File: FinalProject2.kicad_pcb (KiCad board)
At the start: 2 copper layers, 48.3 x 91.4 mm, 22 parts, among them P1 Conn_01x03, P2 Conn_01x02, P3 Conn_01x04, U1 L78L05_TO92, U2 LM339

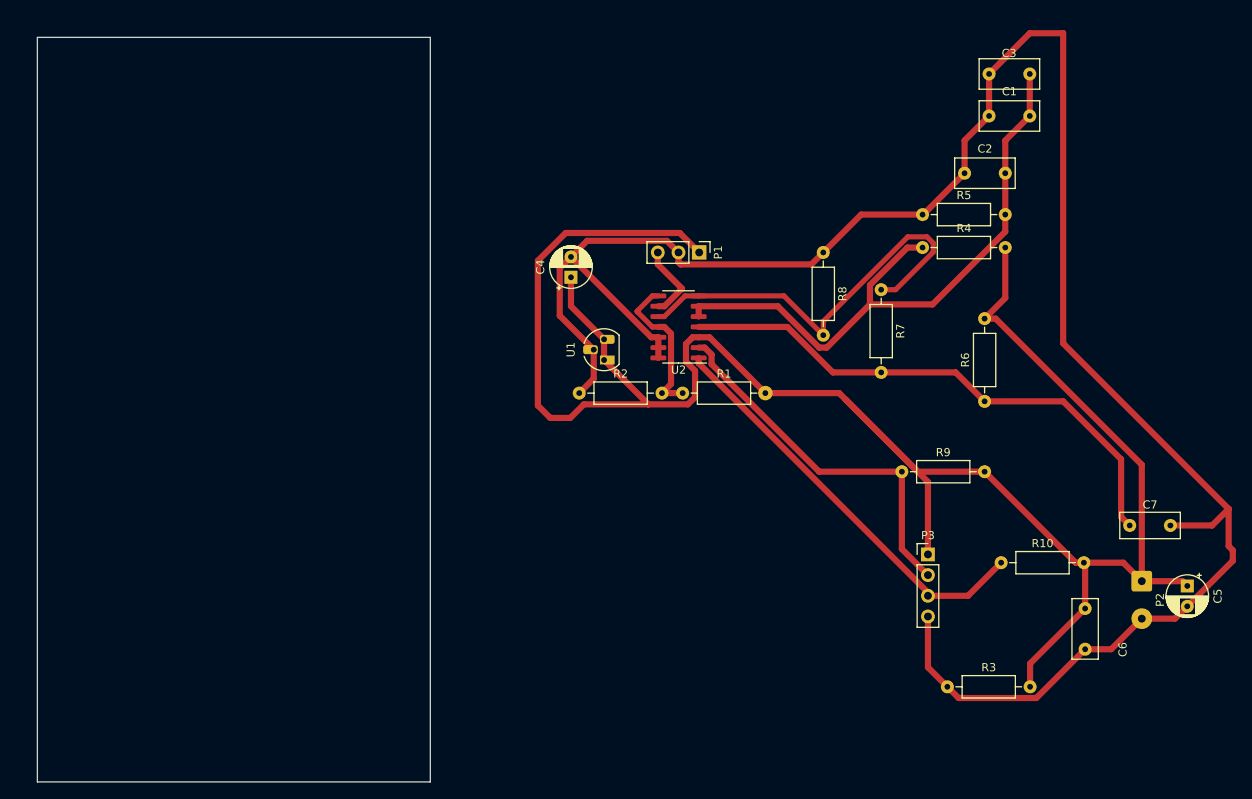
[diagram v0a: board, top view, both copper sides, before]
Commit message: GRN thickness changed to 40mils
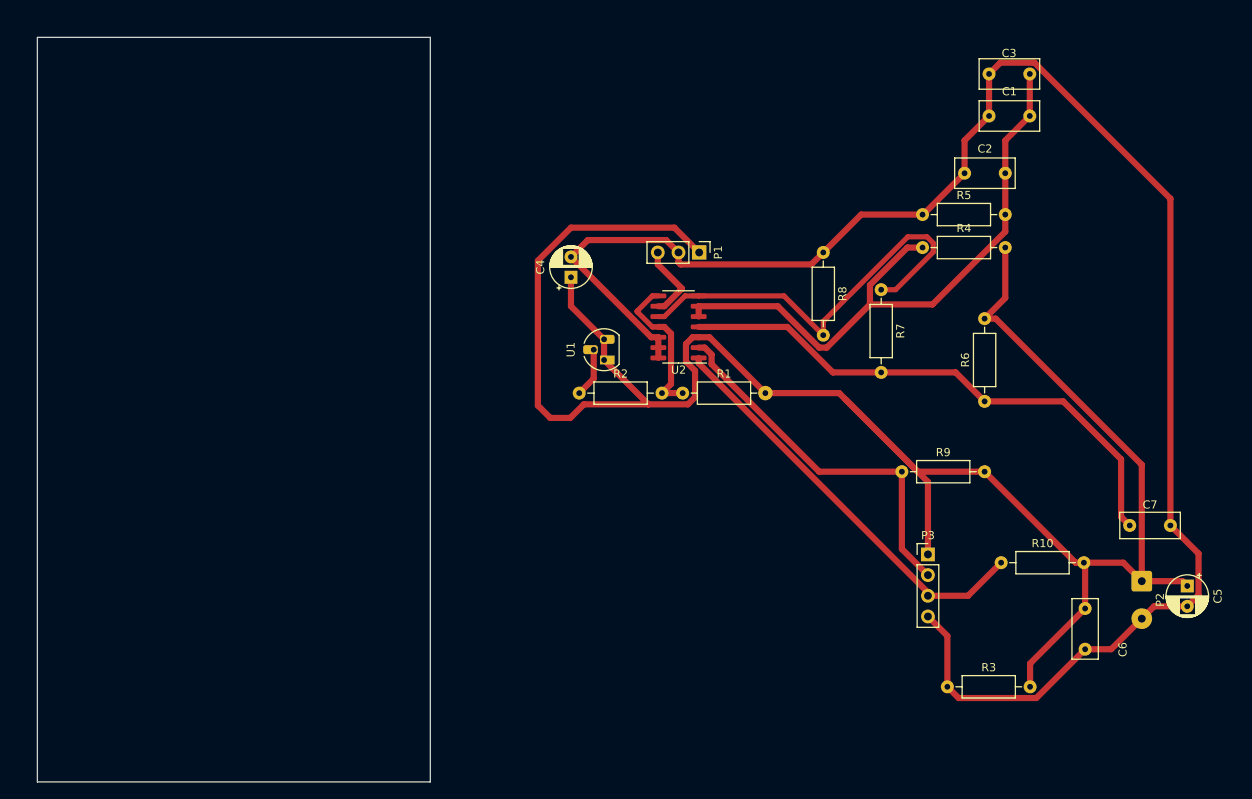
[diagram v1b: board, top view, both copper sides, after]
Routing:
- net GND: track 251.1 -> 218.8 mm
- net Net-(P1-Pin_1): track 254.2 -> 254.8 mm

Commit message: may nakaligtaan akong 1 wire asdasdadsf
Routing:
- net GND: track 218.8 -> 232.5 mm
- net Net-(U2C-+): track 19.0 -> 18.2 mm
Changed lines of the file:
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@@
   (segment (start 277.225 119.293888) (end 275.844 120.674888) (width 0.762) (layer "F.Cu") (net 3))
   (segment (start 270.256 122.188) (end 266.5 125.944) (width 0.762) (layer "F.Cu") (net 3))
+  (segment (start 202.946 89.154) (end 198.771 84.979) (width 0.762) (layer "F.Cu") (net 3))
   (segment (start 202.946 92.71) (end 201.168 94.488) (width 0.762) (layer "F.Cu") (net 3))
+  (segment (start 198.771 84.979) (end 198.771 79.145) (width 0.762) (layer "F.Cu") (net 3))
   (segment (start 231.14 77.216) (end 235.792 72.564) (width 0.762) (layer "F.Cu") (net 3))
   (segment (start 246.38 130.556) (end 246.38 124.306) (width 0.762) (layer "F.Cu") (net 3))
@@
   (segment (start 248.492 63.46) (end 251.5 60.452) (width 0.762) (layer "F.Cu") (net 3))
   (segment (start 210.885 90.17) (end 210.885 87.63) (width 0.762) (layer "F.Cu") (net 3))
+  (segment (start 198.771 79.145) (end 200.152 77.764) (width 0.762) (layer "F.Cu") (net 3))
   (segment (start 251.5 55.292) (end 252.881 53.911) (width 0.762) (layer "F.Cu") (net 3))
   (segment (start 211.836 75.692) (end 213.36 77.216) (width 0.762) (layer "F.Cu") (net 3))
@@
   (segment (start 248.92 119.38) (end 252.984 115.316) (width 0.762) (layer "F.Cu") (net 7))
   (segment (start 215.835 90.818316) (end 243.994 118.977316) (width 0.762) (layer "F.Cu") (net 7))
-  (segment (start 210.14621 86.36) (end 210.885 86.36) (width 0.635) (layer "F.Cu") (net 8))
   (segment (start 211.328 94.488) (end 212.441 93.375) (width 0.762) (layer "F.Cu") (net 8))
   (segment (start 212.441 93.375) (end 212.441 87.17721) (width 0.762) (layer "F.Cu") (net 8))
+  (segment (start 210.885 82.55) (end 210.14621 82.55) (width 0.762) (layer "F.Cu") (net 8))
+  (segment (start 210.14621 82.55) (end 209.296 83.40021) (width 0.762) (layer "F.Cu") (net 8))
   (segment (start 212.441 87.17721) (end 211.62379 86.36) (width 0.762) (layer "F.Cu") (net 8))
-  (segment (start 208.28 84.41621) (end 208.28 84.49379) (width 0.635) (layer "F.Cu") (net 8))
-  (segment (start 210.14621 82.55) (end 208.28 84.41621) (width 0.635) (layer "F.Cu") (net 8))
-  (segment (start 210.885 82.55) (end 210.14621 82.55) (width 0.635) (layer "F.Cu") (net 8))
   (segment (start 213.868 94.488) (end 211.328 94.488) (width 0.762) (layer "F.Cu") (net 8))
   (segment (start 211.62379 86.36) (end 210.885 86.36) (width 0.762) (layer "F.Cu") (net 8))
-  (segment (start 208.28 84.49379) (end 210.14621 86.36) (width 0.635) (layer "F.Cu") (net 8))
-  (segment (start 241.519801 75.2965) (end 243.877727 75.2965) (width 0.635) (layer "F.Cu") (net 9))
-  (segment (start 244.6495 76.068273) (end 244.6495 77.159727) (width 0.635) (layer "F.Cu") (net 9))
-  (segment (start 231.14 85.676301) (end 241.519801 75.2965) (width 0.635) (layer "F.Cu") (net 9))
-  (segment (start 214.16379 82.55) (end 211.62379 85.09) (width 0.635) (layer "F.Cu") (net 9))
-  (segment (start 226.314 82.55) (end 231.14 87.376) (width 0.635) (layer "F.Cu") (net 9))
-  (segment (start 215.835 82.55) (end 214.16379 82.55) (width 0.635) (layer "F.Cu") (net 9))
-  (segment (start 211.62379 85.09) (end 210.885 85.09) (width 0.635) (layer "F.Cu") (net 9))
-  (segment (start 231.14 87.376) (end 231.14 85.676301) (width 0.635) (layer "F.Cu") (net 9))
-  (segment (start 215.835 82.55) (end 226.314 82.55) (width 0.635) (layer "F.Cu") (net 9))
-  (segment (start 244.6495 77.159727) (end 240.021227 81.788) (width 0.635) (layer "F.Cu") (net 9))
-  (segment (start 243.877727 75.2965) (end 244.6495 76.068273) (width 0.635) (layer "F.Cu") (net 9))
-  (segment (start 240.021227 81.788) (end 238.252 81.788) (width 0.635) (layer "F.Cu") (net 9))
+  (segment (start 210.108474 86.36) (end 210.885 86.36) (width 0.762) (layer "F.Cu") (net 8))
+  (segment (start 209.296 83.40021) (end 209.296 85.547526) (width 0.762) (layer "F.Cu") (net 8))
+  (segment (start 209.296 85.547526) (end 210.108474 86.36) (width 0.762) (layer "F.Cu") (net 8))
+  (segment (start 243.904029 75.233) (end 244.713 76.041971) (width 0.762) (layer "F.Cu") (net 9))
+  (segment (start 215.09621 82.55) (end 215.835 82.55) (width 0.762) (layer "F.Cu") (net 9))
+  (segment (start 241.493498 75.233) (end 243.904029 75.233) (width 0.762) (layer "F.Cu") (net 9))
+  (segment (start 240.116029 81.788) (end 238.252 81.788) (width 0.762) (layer "F.Cu") (net 9))
+  (segment (start 212.55621 85.09) (end 215.09621 82.55) (width 0.762) (layer "F.Cu") (net 9))
+  (segment (start 244.713 76.041971) (end 244.713 77.191029) (width 0.762) (layer "F.Cu") (net 9))
+  (segment (start 210.885 85.09) (end 212.55621 85.09) (width 0.762) (layer "F.Cu") (net 9))
+  (segment (start 231.14 85.586498) (end 241.493498 75.233) (width 0.762) (layer "F.Cu") (net 9))
+  (segment (start 231.14 87.376) (end 231.14 85.586498) (width 0.762) (layer "F.Cu") (net 9))
+  (segment (start 226.314 82.55) (end 231.14 87.376) (width 0.762) (layer "F.Cu") (net 9))
+  (segment (start 215.835 82.55) (end 226.314 82.55) (width 0.762) (layer "F.Cu") (net 9))
+  (segment (start 244.713 77.191029) (end 240.116029 81.788) (width 0.762) (layer "F.Cu") (net 9))
 )

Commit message: 40 na yung GRD(2)
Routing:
- net GND: track 232.5 -> 234.9 mm
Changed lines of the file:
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@@
   (segment (start 270.256 103.287527) (end 270.256 117.588) (width 0.762) (layer "F.Cu") (net 2))
   (segment (start 200.152 83.82) (end 204.216 87.884) (width 0.762) (layer "F.Cu") (net 2))
-  (segment (start 277.225 114.197) (end 277.225 119.293888) (width 0.762) (layer "F.Cu") (net 3))
-  (segment (start 273.772 70.610971) (end 273.772 110.744) (width 0.762) (layer "F.Cu") (net 3))
-  (segment (start 213.627919 78.686) (end 229.67 78.686) (width 0.762) (layer "F.Cu") (net 3))
-  (segment (start 251.5 60.452) (end 251.5 55.292) (width 0.762) (layer "F.Cu") (net 3))
-  (segment (start 210.018 87.63) (end 210.885 87.63) (width 0.762) (layer "F.Cu") (net 3))
-  (segment (start 277.225 119.293888) (end 275.844 120.674888) (width 0.762) (layer "F.Cu") (net 3))
-  (segment (start 270.256 122.188) (end 266.5 125.944) (width 0.762) (layer "F.Cu") (net 3))
-  (segment (start 202.946 89.154) (end 198.771 84.979) (width 0.762) (layer "F.Cu") (net 3))
-  (segment (start 202.946 92.71) (end 201.168 94.488) (width 0.762) (layer "F.Cu") (net 3))
-  (segment (start 198.771 84.979) (end 198.771 79.145) (width 0.762) (layer "F.Cu") (net 3))
-  (segment (start 231.14 77.216) (end 235.792 72.564) (width 0.762) (layer "F.Cu") (net 3))
-  (segment (start 246.38 130.556) (end 246.38 124.306) (width 0.762) (layer "F.Cu") (net 3))
-  (segment (start 213.36 78.418081) (end 213.627919 78.686) (width 0.762) (layer "F.Cu") (net 3))
-  (segment (start 202.224 75.692) (end 211.836 75.692) (width 0.762) (layer "F.Cu") (net 3))
-  (segment (start 243.332 72.564) (end 243.412 72.564) (width 0.762) (layer "F.Cu") (net 3))
-  (segment (start 252.881 53.911) (end 257.072029 53.911) (width 0.762) (layer "F.Cu") (net 3))
-  (segment (start 202.946 89.154) (end 202.946 92.71) (width 0.762) (layer "F.Cu") (net 3))
-  (segment (start 213.36 77.216) (end 213.36 78.418081) (width 0.762) (layer "F.Cu") (net 3))
-  (segment (start 229.67 78.686) (end 231.14 77.216) (width 0.762) (layer "F.Cu") (net 3))
-  (segment (start 257.072029 53.911) (end 273.772 70.610971) (width 0.762) (layer "F.Cu") (net 3))
-  (segment (start 247.761 131.937) (end 246.38 130.556) (width 0.762) (layer "F.Cu") (net 3))
-  (segment (start 275.844 120.674888) (end 271.769112 120.674888) (width 0.762) (layer "F.Cu") (net 3))
-  (segment (start 243.412 72.564) (end 248.492 67.484) (width 0.762) (layer "F.Cu") (net 3))
-  (segment (start 273.772 110.744) (end 277.225 114.197) (width 0.762) (layer "F.Cu") (net 3))
-  (segment (start 235.792 72.564) (end 243.332 72.564) (width 0.762) (layer "F.Cu") (net 3))
-  (segment (start 246.38 124.306) (end 243.994 121.92) (width 0.762) (layer "F.Cu") (net 3))
-  (segment (start 271.769112 120.674888) (end 270.256 122.188) (width 0.762) (layer "F.Cu") (net 3))
-  (segment (start 200.152 77.764) (end 210.018 87.63) (width 0.762) (layer "F.Cu") (net 3))
-  (segment (start 200.152 77.764) (end 202.224 75.692) (width 0.762) (layer "F.Cu") (net 3))
-  (segment (start 263.298 125.944) (end 257.305 131.937) (width 0.762) (layer "F.Cu") (net 3))
-  (segment (start 248.492 67.484) (end 248.492 63.46) (width 0.762) (layer "F.Cu") (net 3))
-  (segment (start 257.305 131.937) (end 247.761 131.937) (width 0.762) (layer "F.Cu") (net 3))
-  (segment (start 248.492 63.46) (end 251.5 60.452) (width 0.762) (layer "F.Cu") (net 3))
-  (segment (start 210.885 90.17) (end 210.885 87.63) (width 0.762) (layer "F.Cu") (net 3))
-  (segment (start 198.771 79.145) (end 200.152 77.764) (width 0.762) (layer "F.Cu") (net 3))
-  (segment (start 251.5 55.292) (end 252.881 53.911) (width 0.762) (layer "F.Cu") (net 3))
-  (segment (start 211.836 75.692) (end 213.36 77.216) (width 0.762) (layer "F.Cu") (net 3))
-  (segment (start 266.5 125.944) (end 263.298 125.944) (width 0.762) (layer "F.Cu") (net 3))
+  (segment (start 253.008 53.784) (end 257.124635 53.784) (width 1.016) (layer "F.Cu") (net 3))
+  (segment (start 201.168 90.932) (end 202.946 89.154) (width 1.016) (layer "F.Cu") (net 3))
+  (segment (start 248.492 67.484) (end 248.492 63.46) (width 1.016) (layer "F.Cu") (net 3))
+  (segment (start 257.178 132.064) (end 247.888 132.064) (width 1.016) (layer "F.Cu") (net 3))
+  (segment (start 275.844 120.674888) (end 271.769112 120.674888) (width 1.016) (layer "F.Cu") (net 3))
+  (segment (start 208.207 84.68763) (end 208.207 85.998604) (width 1.016) (layer "F.Cu") (net 3))
+  (segment (start 202.258 75.658) (end 211.802 75.658) (width 1.016) (layer "F.Cu") (net 3))
+  (segment (start 276.97537 120.674888) (end 275.844 120.674888) (width 1.016) (layer "F.Cu") (net 3))
+  (segment (start 213.36 77.216) (end 213.36 77.797) (width 1.016) (layer "F.Cu") (net 3))
+  (segment (start 273.772 70.431365) (end 273.772 110.744) (width 1.016) (layer "F.Cu") (net 3))
+  (segment (start 263.298 125.944) (end 257.178 132.064) (width 1.016) (layer "F.Cu") (net 3))
+  (segment (start 214.376 78.813) (end 229.543 78.813) (width 1.016) (layer "F.Cu") (net 3))
+  (segment (start 198.644 84.852) (end 198.644 78.14063) (width 1.016) (layer "F.Cu") (net 3))
+  (segment (start 200.152 77.764) (end 201.28337 77.764) (width 1.016) (layer "F.Cu") (net 3))
+  (segment (start 201.28337 77.764) (end 208.207 84.68763) (width 1.016) (layer "F.Cu") (net 3))
+  (segment (start 270.256 122.188) (end 267.054 122.188) (width 1.016) (layer "F.Cu") (net 3))
+  (segment (start 248.492 63.46) (end 251.5 60.452) (width 1.016) (layer "F.Cu") (net 3))
+  (segment (start 199.02063 77.764) (end 200.152 77.764) (width 1.016) (layer "F.Cu") (net 3))
+  (segment (start 277.352 114.324) (end 277.352 120.298258) (width 1.016) (layer "F.Cu") (net 3))
+  (segment (start 271.769112 120.674888) (end 270.256 122.188) (width 1.016) (layer "F.Cu") (net 3))
+  (segment (start 247.888 132.064) (end 246.38 130.556) (width 1.016) (layer "F.Cu") (net 3))
+  (segment (start 273.772 110.744) (end 277.352 114.324) (width 1.016) (layer "F.Cu") (net 3))
+  (segment (start 231.14 77.216) (end 235.792 72.564) (width 1.016) (layer "F.Cu") (net 3))
+  (segment (start 267.054 122.188) (end 263.298 125.944) (width 1.016) (layer "F.Cu") (net 3))
+  (segment (start 277.352 120.298258) (end 276.97537 120.674888) (width 1.016) (layer "F.Cu") (net 3))
+  (segment (start 229.543 78.813) (end 231.14 77.216) (width 1.016) (layer "F.Cu") (net 3))
+  (segment (start 210.885 87.63) (end 210.885 90.17) (width 1.016) (layer "F.Cu") (net 3))
+  (segment (start 246.38 130.556) (end 246.38 124.306) (width 1.016) (layer "F.Cu") (net 3))
+  (segment (start 208.207 85.998604) (end 209.838396 87.63) (width 1.016) (layer "F.Cu") (net 3))
+  (segment (start 202.946 89.154) (end 198.644 84.852) (width 1.016) (layer "F.Cu") (net 3))
+  (segment (start 251.5 55.292) (end 253.008 53.784) (width 1.016) (layer "F.Cu") (net 3))
+  (segment (start 246.38 124.306) (end 243.994 121.92) (width 1.016) (layer "F.Cu") (net 3))
+  (segment (start 257.124635 53.784) (end 273.772 70.431365) (width 1.016) (layer "F.Cu") (net 3))
+  (segment (start 213.36 77.797) (end 214.376 78.813) (width 1.016) (layer "F.Cu") (net 3))
+  (segment (start 200.152 77.764) (end 202.258 75.658) (width 1.016) (layer "F.Cu") (net 3))
+  (segment (start 243.332 72.564) (end 243.412 72.564) (width 1.016) (layer "F.Cu") (net 3))
+  (segment (start 211.802 75.658) (end 213.36 77.216) (width 1.016) (layer "F.Cu") (net 3))
+  (segment (start 201.168 94.488) (end 201.168 90.932) (width 1.016) (layer "F.Cu") (net 3))
+  (segment (start 209.838396 87.63) (end 210.885 87.63) (width 1.016) (layer "F.Cu") (net 3))
+  (segment (start 198.644 78.14063) (end 199.02063 77.764) (width 1.016) (layer "F.Cu") (net 3))
+  (segment (start 235.792 72.564) (end 243.332 72.564) (width 1.016) (layer "F.Cu") (net 3))
+  (segment (start 243.412 72.564) (end 248.492 67.484) (width 1.016) (layer "F.Cu") (net 3))
+  (segment (start 251.5 60.452) (end 251.5 55.292) (width 1.016) (layer "F.Cu") (net 3))
   (segment (start 215.835 86.36) (end 226.731526 86.36) (width 0.762) (layer "F.Cu") (net 4))
   (segment (start 232.319526 91.948) (end 238.252 91.948) (width 0.762) (layer "F.Cu") (net 4))

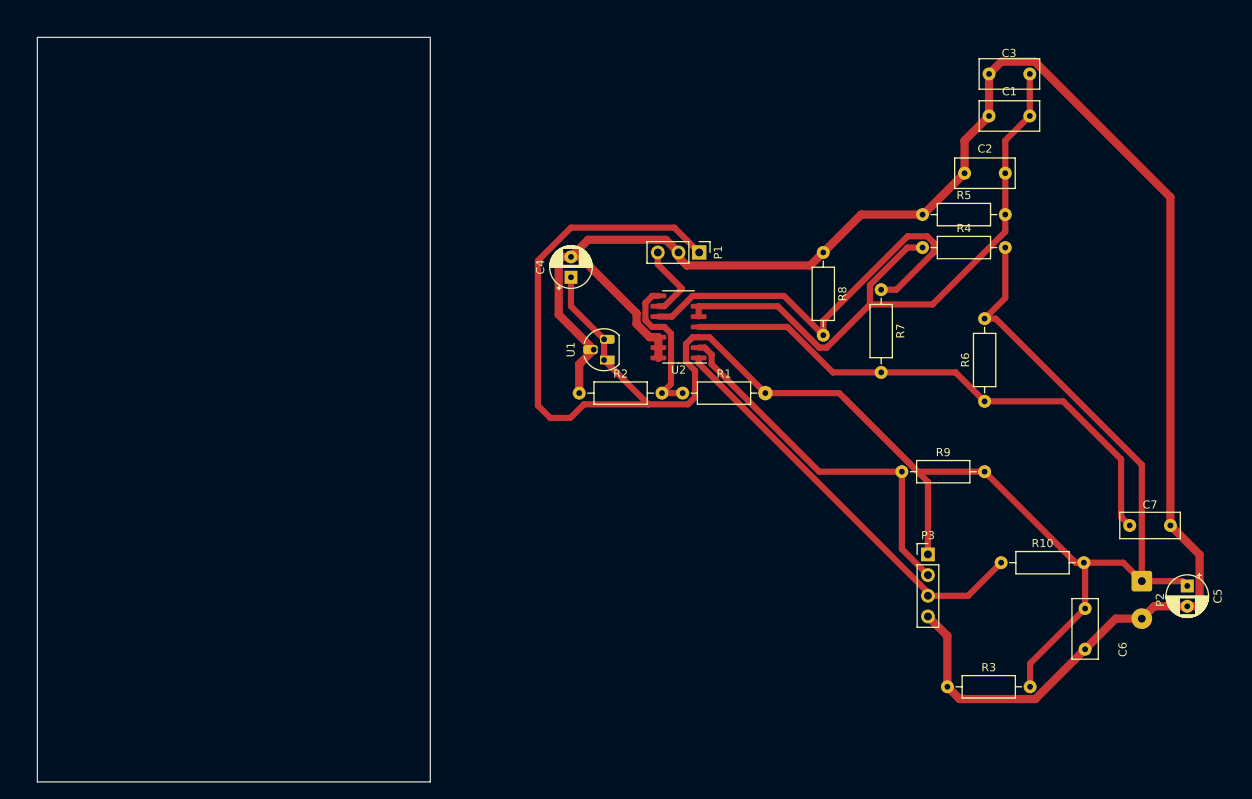
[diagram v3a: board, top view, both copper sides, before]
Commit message: updated PCB tracks
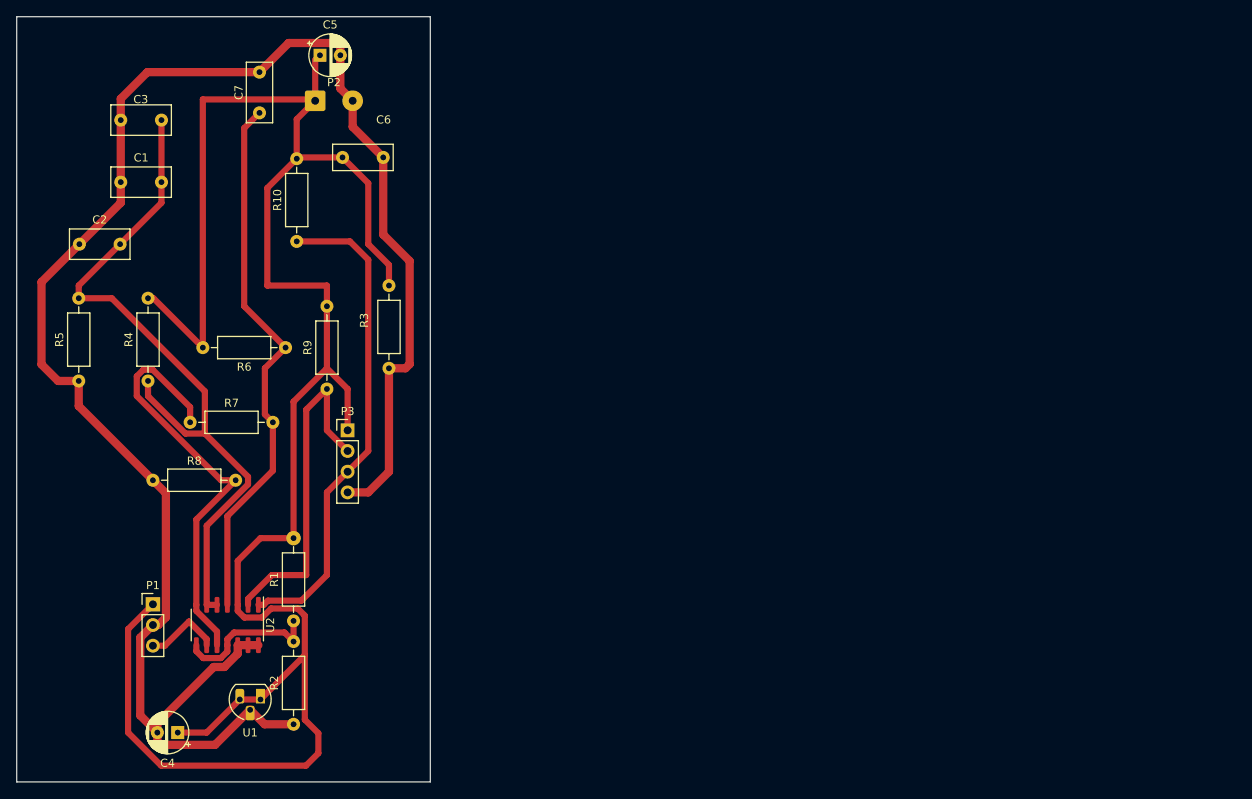
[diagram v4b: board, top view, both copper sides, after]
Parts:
- moved C5 124.9 mm to (169.3, 53.0), turned to 0 degrees
- moved C7 118.3 mm to (161.9, 60.1), turned to 90 degrees
- moved P2 117.4 mm to (168.7, 58.6), turned to 0 degrees
- moved C2 109.1 mm to (139.8, 76.2)
- moved C1 106.9 mm to (144.9, 68.6)
- moved C3 106.8 mm to (144.9, 61.0)
- moved C6 106.7 mm to (172.1, 65.5), turned to 0 degrees
- moved R5 105.6 mm to (139.7, 93.0), turned to 90 degrees
- moved R4 96.5 mm to (148.2, 93.0), turned to 90 degrees
- moved R10 95.1 mm to (166.5, 75.9), turned to 90 degrees
- moved R8 87.0 mm to (148.8, 105.2), turned to 0 degrees
- moved R7 86.4 mm to (153.4, 98.1), turned to 0 degrees
- moved R6 86.1 mm to (165.1, 88.9), turned to 180 degrees
- moved P1 79.8 mm to (148.8, 120.4), turned to 0 degrees
- moved R3 79.0 mm to (177.8, 91.4), turned to 90 degrees
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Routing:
- net Net-(U2A-+): track 78.3 -> 88.9 mm
- net GND: track 234.9 -> 225.0 mm
- net Net-(P3-Pin_3): track 51.5 -> 60.5 mm
- net Net-(P1-Pin_1): track 254.8 -> 260.4 mm
- net Net-(P3-Pin_2): track 46.0 -> 41.7 mm
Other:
- board size 48.3 x 91.4 mm -> 50.8 x 94 mm
